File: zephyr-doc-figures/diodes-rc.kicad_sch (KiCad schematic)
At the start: 18 parts, among them SW1 SW_Push

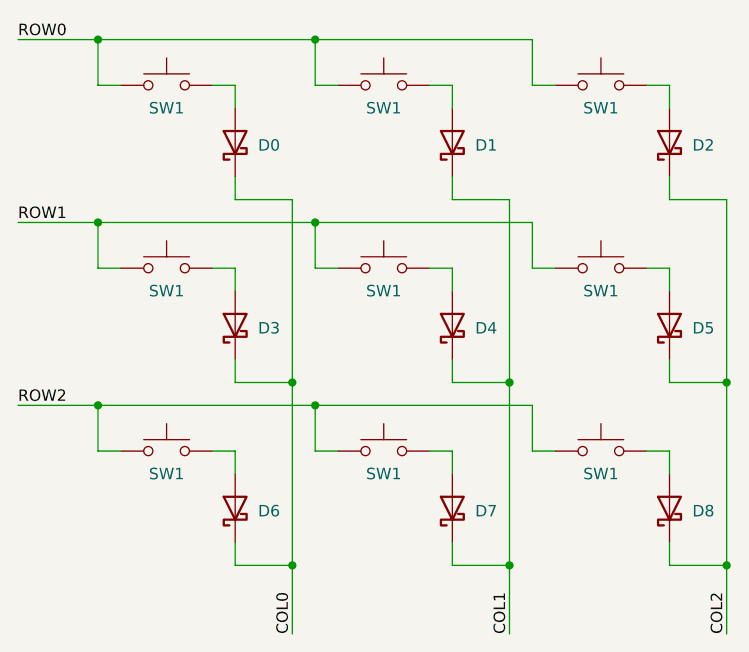
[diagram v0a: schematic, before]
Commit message: zephyr-doc-figures: update style and refdes
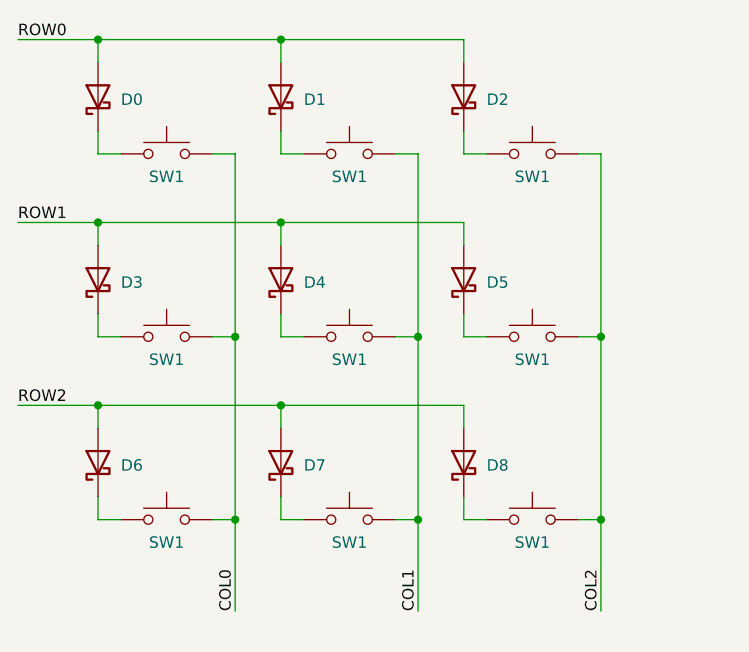
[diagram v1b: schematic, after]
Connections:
- net COL0: now also SW1.2, SW1.2, SW1.2; no longer D0.1 (K), D3.1 (K), D6.1 (K)
- net COL1: now also SW1.2, SW1.2, SW1.2; no longer D1.1 (K), D4.1 (K), D7.1 (K)
- net COL2: now also SW1.2, SW1.2, SW1.2; no longer D2.1 (K), D5.1 (K), D8.1 (K)
- net ROW0: now also D0.2 (A), D1.2 (A), D2.2 (A); no longer SW1.1, SW1.1, SW1.1
- net ROW1: now also D3.2 (A), D4.2 (A), D5.2 (A); no longer SW1.1, SW1.1, SW1.1
- net ROW2: now also D6.2 (A), D7.2 (A), D8.2 (A); no longer SW1.1, SW1.1, SW1.1
- new net: D5.1 (K), SW1.1
- new net: D1.1 (K), SW1.1
- new net: D6.1 (K), SW1.1
- new net: D4.1 (K), SW1.1
- new net: D0.1 (K), SW1.1
- new net: D7.1 (K), SW1.1
- new net: D2.1 (K), SW1.1
- new net: D8.1 (K), SW1.1
- new net: D3.1 (K), SW1.1
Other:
- moved on the sheet: D0, D1, D2, D3, D4, D5, D6, D7, D8, SW1
